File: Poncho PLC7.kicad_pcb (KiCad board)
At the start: 2 copper layers, 135.6 x 83.3 mm, 99 parts, among them J1 TB_1X2-PonchoPLC-rescue, J10 Conn_02x12_Odd_Even, J13 Conn_02x05_Odd_Even, J18 Conn_02x05_Odd_Even, J2 TB_1X3-PonchoPLC-rescue, J3 TB_1X2, J4 TB_1X2, J5 TB_1X2, J6 TB_1X2, J7 Conn_02x12_Odd_Even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

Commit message: Esq + PCB + Bom terminados
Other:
- board text added: "PONCHO PLC7 Diseñado en ARGENTINA"

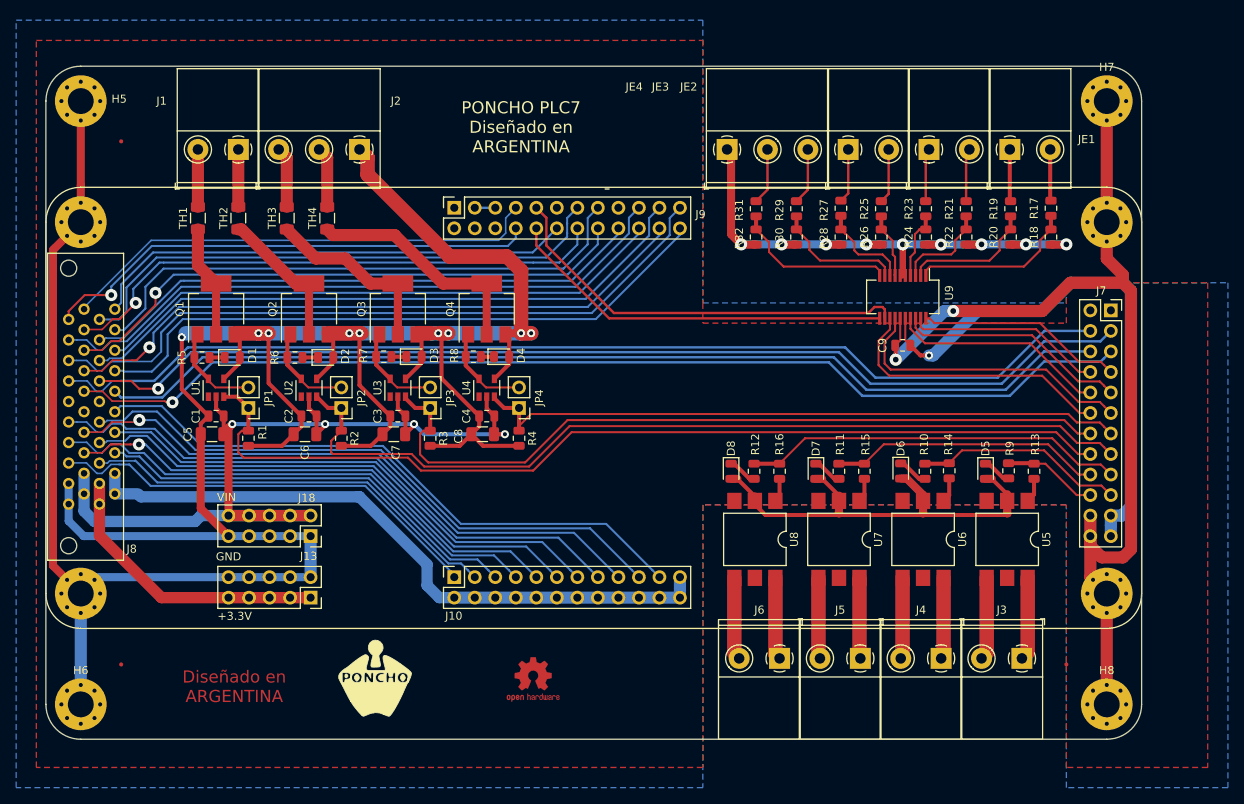
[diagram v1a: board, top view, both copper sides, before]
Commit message: Agregado Leds Entradas
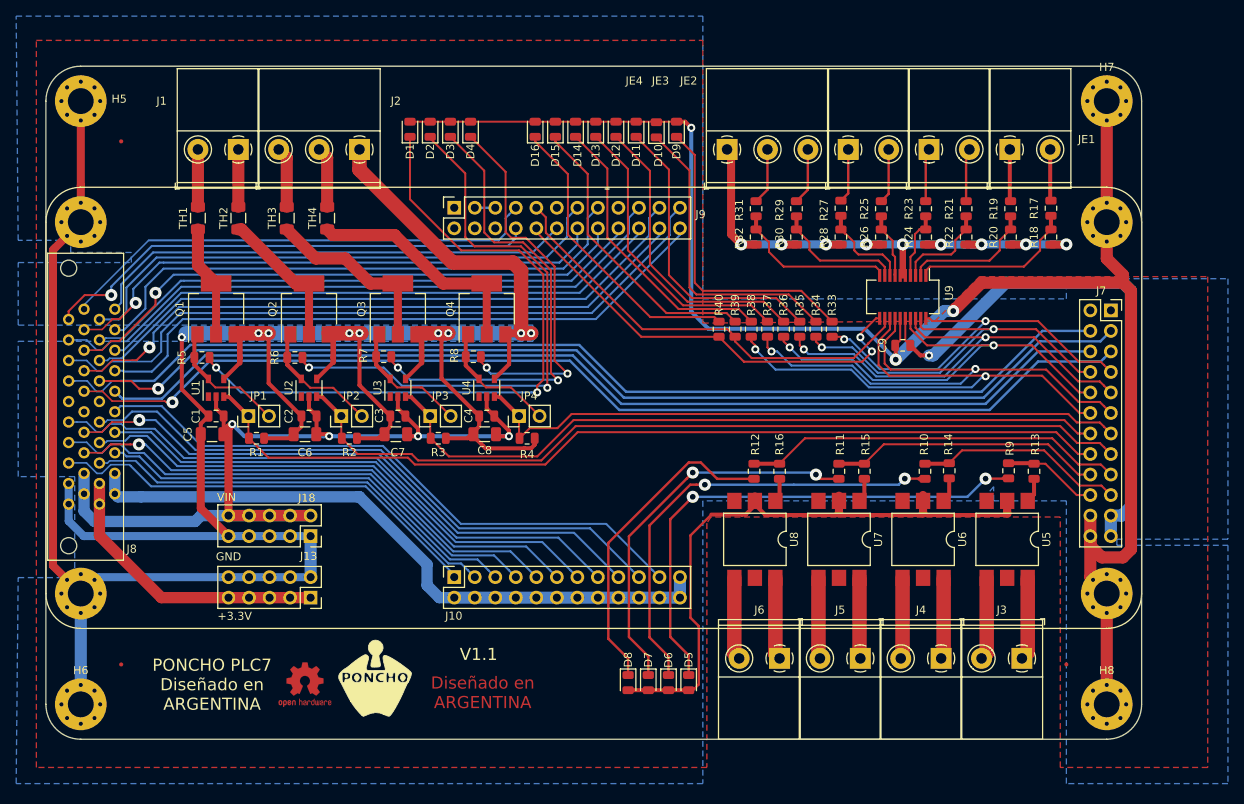
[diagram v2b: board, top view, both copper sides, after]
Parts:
- added D10: LED red, LED_SMD:LED_0805_2012Metric, F.Cu at (109.2, 68.6)
- added D11: LED red, LED_SMD:LED_0805_2012Metric, F.Cu at (106.8, 68.5)
- added D12: LED red, LED_SMD:LED_0805_2012Metric, F.Cu at (104.2, 68.5)
- added D13: LED red, LED_SMD:LED_0805_2012Metric, F.Cu at (101.8, 68.5)
- added D14: LED red, LED_SMD:LED_0805_2012Metric, F.Cu at (99.2, 68.5)
- added D15: LED red, LED_SMD:LED_0805_2012Metric, F.Cu at (96.8, 68.5)
- added D16: LED red, LED_SMD:LED_0805_2012Metric, F.Cu at (94.2, 68.5)
- added D9: LED red, LED_SMD:LED_0805_2012Metric, F.Cu at (111.8, 68.5)
- added R33: 330, Resistor_SMD:R_0805_2012Metric, F.Cu at (131.0, 93.2)
- added R34: 330, Resistor_SMD:R_0805_2012Metric, F.Cu at (129.0, 93.2)
- added R35: 330, Resistor_SMD:R_0805_2012Metric, F.Cu at (127.0, 93.2)
- added R36: 330, Resistor_SMD:R_0805_2012Metric, F.Cu at (125.0, 93.2)
- added R37: 330, Resistor_SMD:R_0805_2012Metric, F.Cu at (123.0, 93.2)
- added R38: 330, Resistor_SMD:R_0805_2012Metric, F.Cu at (121.0, 93.2)
- added R39: 330, Resistor_SMD:R_0805_2012Metric, F.Cu at (119.0, 93.2)
- added R40: 330, Resistor_SMD:R_0805_2012Metric, F.Cu at (117.0, 93.2)
- J3, J4, J5, J6: value TB_1X2 -> TB_1X3-PonchoPLC-rescue
- JE1, JE2, JE3: value TB_1X2 -> TB_1X2-PonchoPLC-rescue
- JE4: value TB_1X3 -> TB_1X3-PonchoPLC-rescue
- moved D5 45.1 mm to (113.2, 137.0)
- moved D6 38.9 mm to (110.8, 137.0)
- moved D1 35.8 mm to (78.8, 68.5), turned to 90 degrees
- moved D7 33.4 mm to (108.2, 137.0)
- moved D2 31.1 mm to (81.2, 68.5), turned to 90 degrees
- moved D8 29.1 mm to (105.8, 137.0)
- moved D3 28.5 mm to (83.8, 68.5), turned to 90 degrees
- moved D4 28.4 mm to (86.2, 68.5), turned to 90 degrees
- moved   28.3 mm to (65.8, 137.2)
- moved JP1 1.00 mm to (58.8, 104.0), turned to 90 degrees
- moved JP2 1.00 mm to (70.2, 104.0), turned to 90 degrees
- moved JP3 1.00 mm to (81.2, 104.0), turned to 90 degrees
- moved JP4 1.00 mm to (92.2, 104.0), turned to 90 degrees
- moved R1 1.00 mm to (59.8, 106.8), turned to 0 degrees
- moved R2 1.00 mm to (71.2, 106.8), turned to 0 degrees
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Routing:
- net GND: track 544.7 -> 648.9 mm, vias 11 -> 12
- net Net-(D1-Pad1): track 1.88 -> 85.9 mm, vias 0 -> 2
- net Net-(D2-Pad1): track 1.94 -> 72.6 mm, vias 0 -> 2
- net Net-(D5-Pad1): track 3.59 -> 64.8 mm, vias 0 -> 2
- net Net-(D3-Pad1): track 1.88 -> 60.0 mm, vias 0 -> 2
- net Net-(D6-Pad1): track 3.79 -> 56.7 mm, vias 0 -> 2
- net Net-(D4-Pad1): track 1.62 -> 47.4 mm, vias 0 -> 2
- net Net-(D7-Pad1): track 3.62 -> 48.3 mm, vias 0 -> 2
- net Net-(D9-Pad1): track 0.00 -> 38.0 mm
- net Net-(D10-Pad1): track 0.00 -> 37.7 mm
- net Net-(D11-Pad1): track 0.00 -> 37.4 mm
- net Net-(D8-Pad1): track 3.62 -> 41.0 mm
- net Net-(D12-Pad1): track 0.00 -> 37.0 mm
- net Net-(D16-Pad1): track 0.00 -> 36.9 mm
- net Net-(D13-Pad1): track 0.00 -> 36.6 mm
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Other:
- net class FinePitch: via_dia 1.5 -> 1; via_drill 0.7 -> 0.5
- net class UltraFinePitch: via_dia 1.5 -> 1
- board text added: "V1.1"
